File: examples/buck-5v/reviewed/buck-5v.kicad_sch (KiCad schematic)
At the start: 17 parts, among them J1 12V IN, J2 5V OUT, U1 LM2596S-5

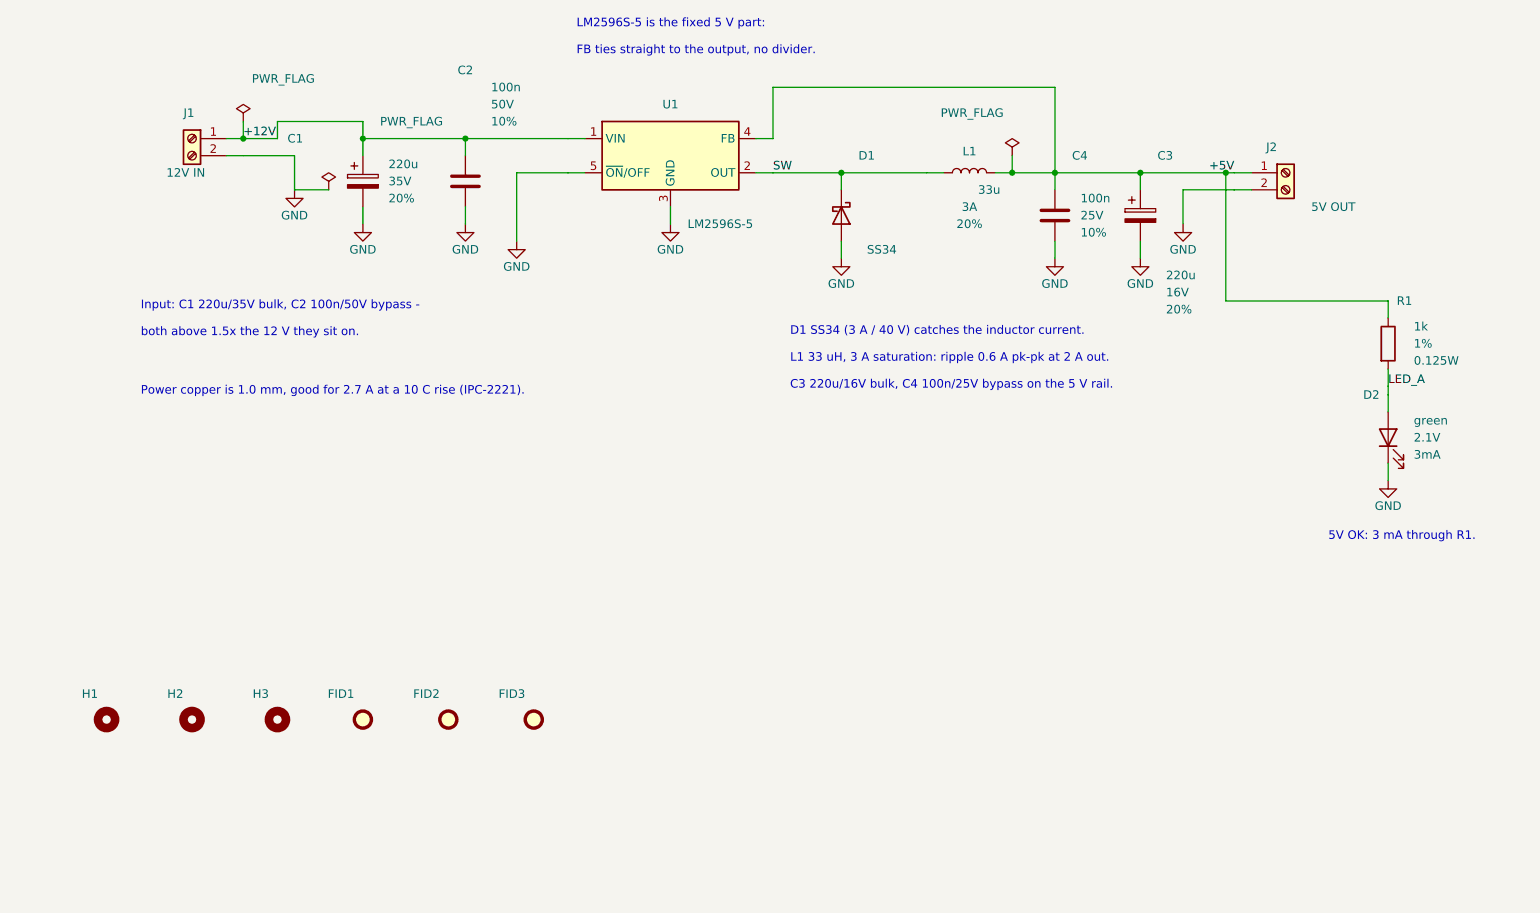
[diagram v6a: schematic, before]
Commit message: feat(examples): round twenty - fuse and clamp every input, state the ESR, damp the clock, control the mute
Redesign of the five worked examples for the items REVIEW.md left open:

- every power input gets a fuse in series and a TVS across the fused rail
  (a resettable fuse on the Pico carrier, whose Schottky already blocks a
  reversed supply); each sheet states what the clamp does not do
- the buck's output capacitor states the ESR the LM2596 loop is designed
  around (SNVS124G 9.1.3), derived from the ripple already on the sheet
- the FPGA's 12 MHz clock leaves its oscillator through 33 ohms
- the DAC's XSMT is driven from the FPGA with a pull-down instead of
  strapped high, so it comes up muted
- the op-amp filter's output goes through a 100 ohm isolation resistor

Generator fixes the round found: _surfaced pruned a via that tapped the
middle of a back-layer spine, and _chamfer_tracks cut the copper out from
under a via sitting a fraction along a leg; both left a net in two pieces
that KiCad's DRC reported. Pin stubs closer than 7.62 mm draw over each
other, so the new parts are spaced for it and the comments say why.

tools/example_images.py renders the README pictures from the regenerated
projects. All five reviewed variants pass their gates and KiCad's DRC on
both matrix versions; the as-generated variants each carry one more
blocking finding (spec.missing_esr). REVIEW.md 25 records the round.

Co-Authored-By: Claude Fable 5.1 <noreply@anthropic.com>
Claude-Session: https://claude.ai/code/session_017JKofiLFxXjzRRnBmFyXuQ
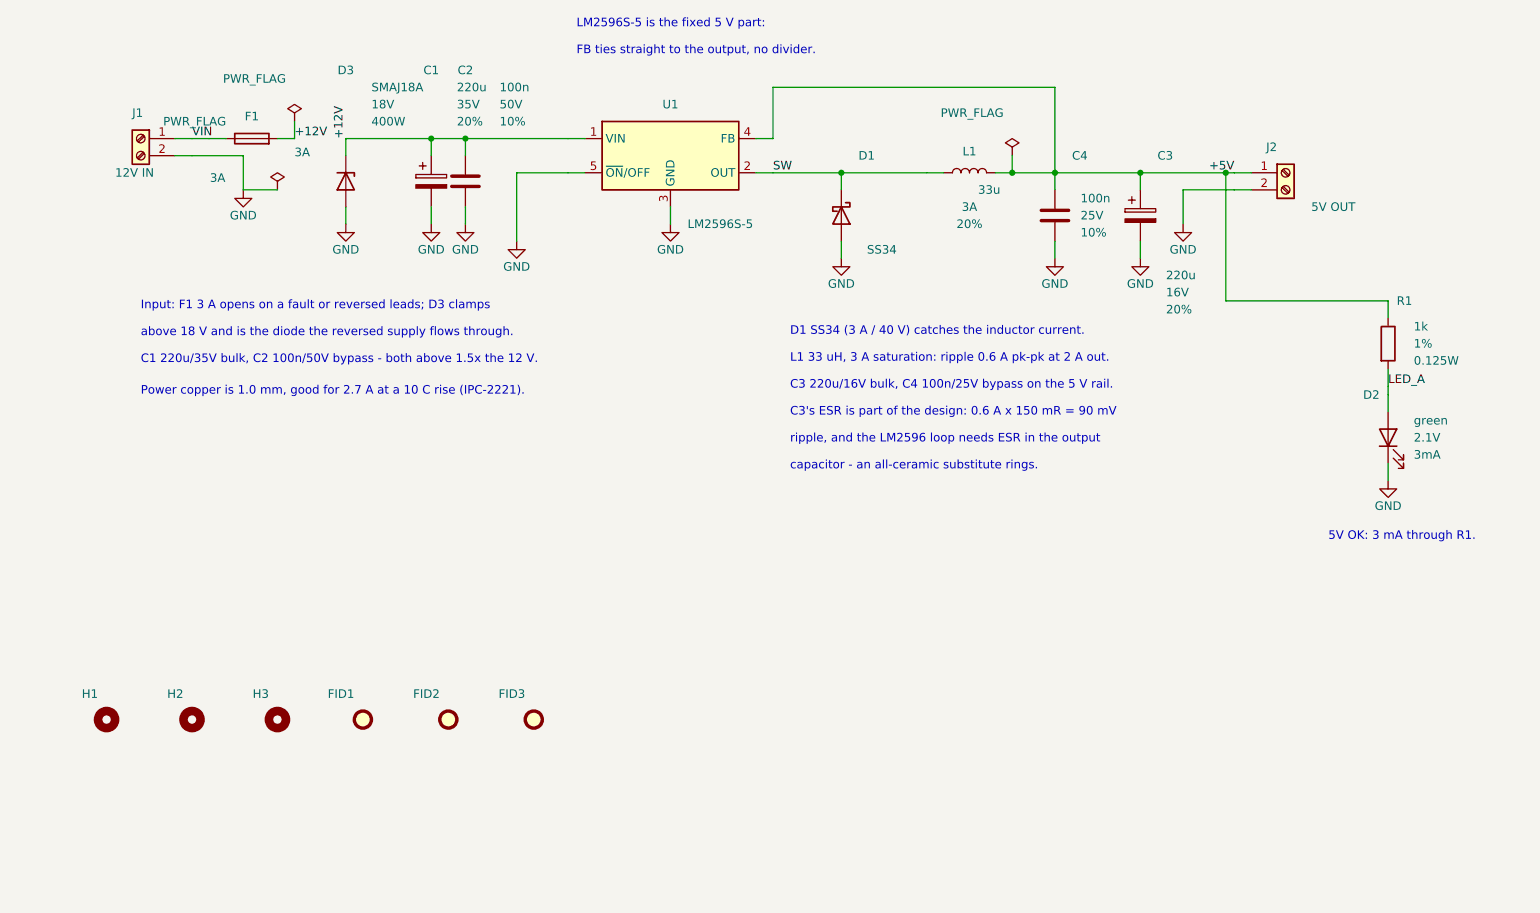
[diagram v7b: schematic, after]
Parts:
- added D3: SMAJ18A, Diode_SMD:D_SMA, symbol Device:D_Zener
- added F1: 3A, Fuse:Fuse_1206_3216Metric, symbol Device:Fuse
- C3: ESR (none) -> 150mR max @100kHz
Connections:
- net +12V: now also D3.1 (K), F1.2; no longer J1.1 (Pin_1)
- net GND: now also D3.2 (A)
- new net VIN: F1.1, J1.1 (Pin_1)
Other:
- note added: "C1 220u/35V bulk, C2 100n/50V bypass - both above 1.5x the 12 V."
- note added: "C3's ESR is part of the design: 0.6 A x 150 mR = 90 mV"
- note added: "Input: F1 3 A opens on a fault or reversed leads; D3 clamps"
- note added: "above 18 V and is the diode the reversed supply flows through."
- note added: "capacitor - an all-ceramic substitute rings."
- note added: "ripple, and the LM2596 loop needs ESR in the output"
- note removed: "Input: C1 220u/35V bulk, C2 100n/50V bypass -"
- note removed: "both above 1.5x the 12 V they sit on."
- moved on the sheet: C1, J1
